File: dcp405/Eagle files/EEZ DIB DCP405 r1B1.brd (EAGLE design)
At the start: 185 x 95 mm, 321 parts, among them IC1 LTC3864EMSE#PBF, IC10 OPA2196ID, IC11 MC33272ADR2G, IC12 LTC2050HVCS8#PBF, IC13 74AUP1G74DC.125, IC14 MCP23S17-E/SS, IC15 REF5025AIDR, IC16 DAC8552IDGKR, IC17 SN74LVC1G3157DCKR, IC18 ADS1120IPWR, IC19 LM339D, IC2 TL783CKCSE3, IC20 MAX9141ESA, IC3 LP2951, IC4 SI8641BB-B-IS1, IC5 SN74LVC1G139DCUR, IC6 LTC3260EMSE#PBF, IC7 SI8641BB-B-IS1, IC8 M24C32-WMN6P, IC9 TMP1075AIDGK, J1 4907, J2 FCR7350R, J3 FCR7350B, K1 G6K-2F-5DC, Q1 SUD19P06-60, Q10 MMBT5551, Q11 MMBT5551, Q12 PSMN0R9-25YLC, Q13 PSMN0R9-25YLC, Q14 PSMN0R9-25YLC, Q15 2N7002, Q16 BSS84P, Q17 BTA26-600, Q18 FMMT493TA, Q19 2N7002, Q2 MMBT5401, Q20 2N7002, Q21 2N7002, Q22 MMBT5551, Q23 MMBT5401, Q24 MMBT5551, Q25 MMBT5551, Q26 2N7002, Q3 IRFP250MPBF, Q4 BC856C, Q5 BCP56-16.115, Q6 STF10P6F6, Q7 BCP56-16.115, Q8 MMBT5401, Q9 MMBT5401, X1 39-30-1020, X2 M20-9701346, X3 1844249, X4 ZL263-20DG

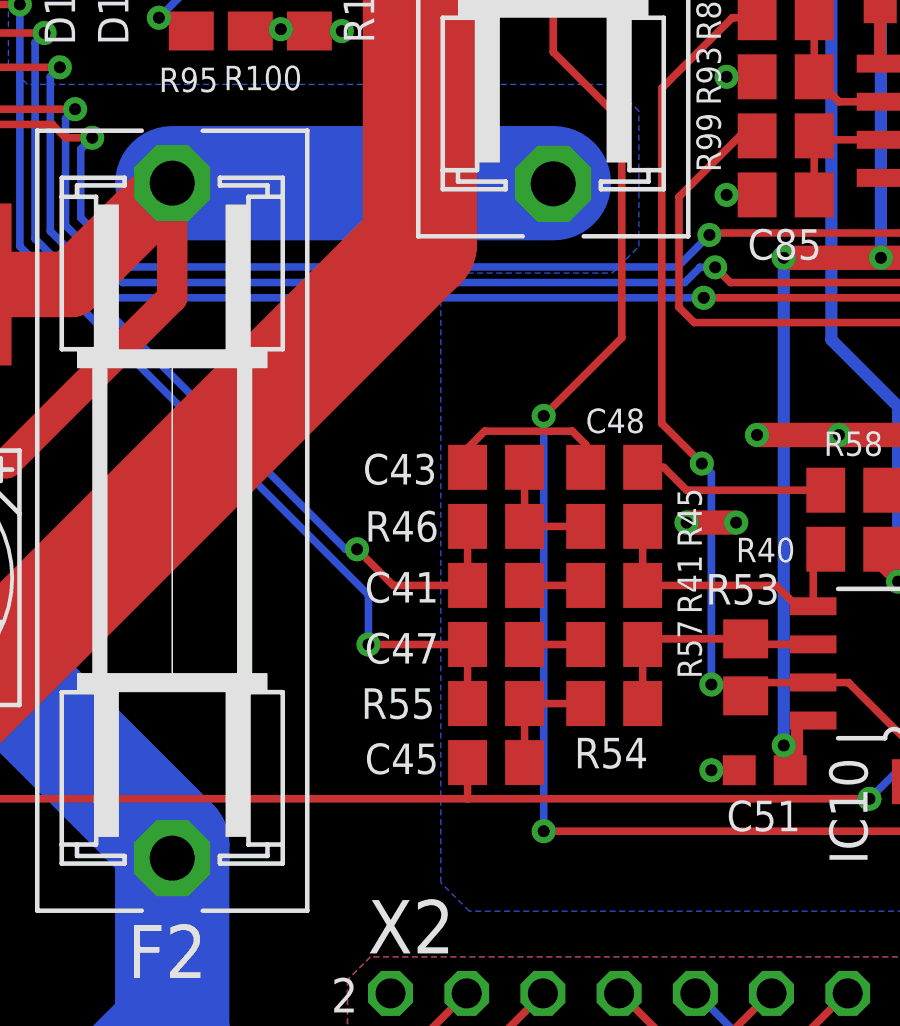
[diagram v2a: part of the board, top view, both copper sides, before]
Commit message: DCP405 JP3, JP4 added
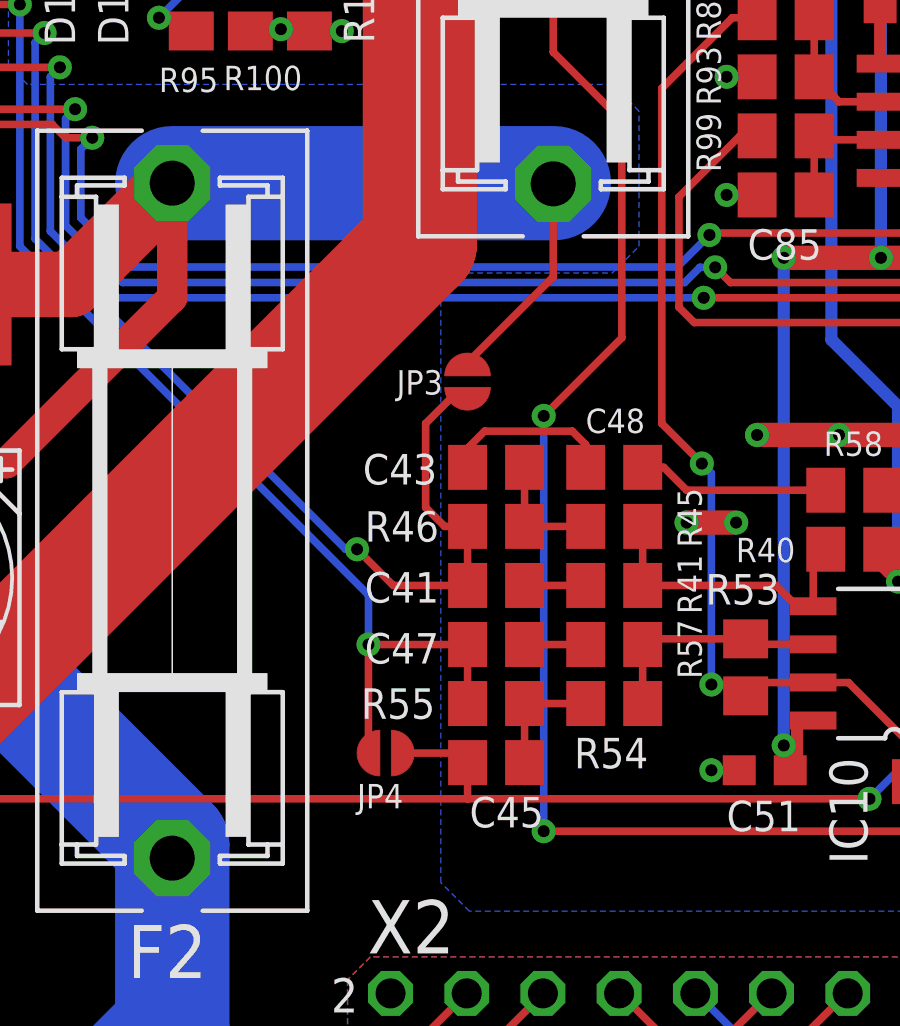
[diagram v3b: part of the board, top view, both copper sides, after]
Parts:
- added JP3, JP4: JP2-CUT, EEZ_Lib1:JP2-CUT
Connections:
- net POST_OUT-: now also JP4.1
- net POST_OUTF+: now also JP3.2
- net SENSE+: now also JP3.1
- net SENSE-: now also JP4.2
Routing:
- net POST_OUTF+: track 97.0 -> 104.2 mm
- net SENSE+: track 72.8 -> 79.1 mm
- net SENSE-: track 71.2 -> 74.8 mm
- net POST_OUT-: track 229.2 -> 231.6 mm
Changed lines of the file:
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@@
 <layer number="24" name="bOrigins" color="15" fill="1" visible="no" active="yes"/>
 <layer number="25" name="tNames" color="7" fill="1" visible="yes" active="yes"/>
-<layer number="26" name="bNames" color="5" fill="1" visible="yes" active="yes"/>
+<layer number="26" name="bNames" color="5" fill="1" visible="no" active="yes"/>
 <layer number="27" name="tValues" color="14" fill="1" visible="no" active="yes"/>
 <layer number="28" name="bValues" color="10" fill="1" visible="no" active="yes"/>
@@
 </element>
 <element name="C45" library="rcl" package="C0805" value="2n2" x="58.039" y="20.193" smashed="yes" rot="R180">
-<attribute name="NAME" x="56.134" y="20.828" size="1.016" layer="25" ratio="10" rot="R180"/>
+<attribute name="NAME" x="59.6265" y="19.05" size="1.016" layer="25" ratio="10" rot="R180"/>
 <attribute name="VALUE" x="59.563" y="20.6375" size="1.016" layer="27" ratio="10" rot="R180"/>
 </element>
@@
 <element name="C66" library="EEZ_Lib1" package="EC1206" value="4u7 tant." x="101.6635" y="24.511" smashed="yes">
 <attribute name="NAME" x="100.33" y="25.781" size="1.016" layer="25" ratio="10"/>
-<attribute name="VALUE" x="100.2665" y="24.003" size="1.016" layer="27" ratio="10"/>
+<attribute name="VALUE" x="99.06" y="24.1935" size="0.8128" layer="27" ratio="10"/>
 </element>
 <element name="C79" library="rcl" package="C0603" value="100n" x="113.6015" y="26.543" smashed="yes" rot="R270">
@@
 <attribute name="TME" value="MCP23S17-E/SS" x="336.804" y="17.653" size="1.778" layer="27" rot="R90" display="off"/>
 <attribute name="NAME" x="144.3101" y="57.9755" size="1.27" layer="25" ratio="10" rot="SR0"/>
-<attribute name="VALUE" x="148.5265" y="53.6829" size="0.8128" layer="27" ratio="10" rot="SR180"/>
+<attribute name="VALUE" x="139.0015" y="52.9336" size="0.8128" layer="27" ratio="10" rot="SR0"/>
 </element>
 <element name="R78" library="rcl" package="R0805" value="270R" x="12.5095" y="31.5265" smashed="yes" rot="R90">
@@
 <element name="C6" library="rcl" package="C1210" value="4u7/100V" x="168.91" y="56.388" smashed="yes" rot="R90">
 <attribute name="NAME" x="168.2115" y="59.055" size="1.016" layer="25" ratio="10"/>
-<attribute name="VALUE" x="169.545" y="54.991" size="1.016" layer="27" ratio="10" rot="R90"/>
+<attribute name="VALUE" x="169.418" y="53.721" size="0.8128" layer="27" ratio="10" rot="R90"/>
 </element>
 <element name="C10" library="rcl" package="C1210" value="10u" x="169.7355" y="67.056" smashed="yes" rot="R270">
@@
 <element name="C5" library="rcl" package="C1210" value="4u7/100V" x="172.1485" y="56.388" smashed="yes" rot="R90">
 <attribute name="NAME" x="171.45" y="59.055" size="1.016" layer="25" ratio="10"/>
-<attribute name="VALUE" x="172.593" y="55.0545" size="1.016" layer="27" ratio="10" rot="R90"/>
+<attribute name="VALUE" x="172.593" y="53.6575" size="0.8128" layer="27" ratio="10" rot="R90"/>
 </element>
 <element name="D2" library="EEZ_Lib1" package="TO252-L" value="STPS15H100" x="158.3055" y="58.6105" smashed="yes" rot="R90">
 <attribute name="NAME" x="154.051" y="59.1185" size="1.27" layer="25" ratio="10" rot="R180"/>
-<attribute name="VALUE" x="165.354" y="59.309" size="1.016" layer="27" ratio="10" rot="R180"/>
+<attribute name="VALUE" x="161.798" y="60.579" size="1.016" layer="27" ratio="10" rot="R180"/>
 </element>
 <element name="R4" library="rcl" package="R0805" value="47K" x="166.243" y="38.4175" smashed="yes" rot="R180">
@@
 <element name="Q1" library="EEZ_Lib1" package="TO229P990X239-3N" value="SUD19P06-60" x="158.3055" y="49.911" smashed="yes" rot="R90">
 <attribute name="NAME" x="154.8765" y="50.546" size="1.27" layer="25" ratio="10" rot="R180"/>
-<attribute name="VALUE" x="161.4805" y="50.4825" size="1.016" layer="27" ratio="10" rot="R180"/>
+<attribute name="VALUE" x="161.6075" y="51.7525" size="1.016" layer="27" ratio="10" rot="R180"/>
 </element>
 <element name="IC1" library="EEZ_Lib1" package="LTC_05-08-1666" value="LTC3864EMSE#PBF" x="170.815" y="42.6085" smashed="yes" rot="R90">
@@
 <element name="FB2" library="EEZ_Lib1" package="BEAD0603" value="60R@100MHz" x="149.1615" y="3.1115" smashed="yes" rot="R180">
 <attribute name="NAME" x="150.627" y="2.648" size="1.016" layer="25" ratio="10"/>
-<attribute name="VALUE" x="147.7505" y="2.7245" size="0.8128" layer="27" ratio="10"/>
+<attribute name="VALUE" x="147.7505" y="2.28" size="0.8128" layer="27" ratio="10"/>
 </element>
 <element name="R21" library="rcl" package="R0805" value="100K" x="157.48" y="9.017" smashed="yes">
@@
 <element name="C4" library="rcl" package="C1206" value="4n7/100V" x="161.29" y="21.2725" smashed="yes" rot="R270">
 <attribute name="NAME" x="158.9405" y="22.7965" size="1.016" layer="25" ratio="10" rot="R270"/>
-<attribute name="VALUE" x="161.8615" y="16.383" size="1.016" layer="27" ratio="10" rot="R90"/>
+<attribute name="VALUE" x="161.671" y="17.907" size="0.8128" layer="27" ratio="10" rot="R90"/>
 </element>
 <element name="C3" library="rcl" package="C1206" value="4n7/100V" x="161.29" y="26.67" smashed="yes" rot="R270">
 <attribute name="NAME" x="161.798" y="29.4005" size="1.27" layer="25" ratio="10" rot="R90"/>
-<attribute name="VALUE" x="160.7185" y="31.8135" size="1.016" layer="27" ratio="10" rot="R270"/>
+<attribute name="VALUE" x="160.782" y="30.226" size="0.8128" layer="27" ratio="10" rot="R270"/>
 </element>
 <element name="C1" library="rcl" package="C1206" value="4n7/100V" x="182.626" y="23.622" smashed="yes" rot="R270">
@@
 <element name="C12" library="rcl" package="C0805" value="n.c." x="162.433" y="85.6615" smashed="yes" rot="R270">
 <attribute name="NAME" x="162.8775" y="87.8205" size="1.016" layer="25" ratio="10" rot="R90"/>
-<attribute name="VALUE" x="162.052" y="87.1855" size="1.27" layer="27" rot="R270"/>
+<attribute name="VALUE" x="161.6075" y="87.5665" size="1.27" layer="27" rot="R270"/>
 </element>
 <element name="C33" library="rcl" package="C1210" value="10u" x="150.4315" y="20.447" smashed="yes">
@@
 <element name="C27" library="EEZ_Lib1" package="EC1206" value="10u tant." x="155.6385" y="4.3815" smashed="yes">
 <attribute name="NAME" x="158.242" y="4.0005" size="1.016" layer="25" ratio="10"/>
-<attribute name="VALUE" x="156.7815" y="4.7625" size="1.016" layer="27" ratio="10" rot="R180"/>
+<attribute name="VALUE" x="153.4795" y="3.937" size="1.016" layer="27" ratio="10"/>
 </element>
 <element name="C34" library="EEZ_Lib1" package="EC1206" value="10u tant." x="155.6385" y="21.9075" smashed="yes" rot="R180">
 <attribute name="NAME" x="153.162" y="23.114" size="1.016" layer="25" ratio="10"/>
-<attribute name="VALUE" x="157.2895" y="22.4155" size="1.27" layer="27" ratio="10" rot="R180"/>
+<attribute name="VALUE" x="159.3215" y="22.4155" size="0.8128" layer="27" ratio="10" rot="R180"/>
 </element>
 <element name="C21" library="rcl" package="C0603" value="100n" x="157.4165" y="37.846" smashed="yes" rot="R270">
@@
 <attribute name="NAME" x="72.771" y="29.7815" size="0.8128" layer="25" ratio="10"/>
 </element>
+<element name="JP3" library="EEZ_Lib1" package="JP2-CUT" value="JP2-CUT" x="57.0865" y="32.893" smashed="yes" rot="R90">
+<attribute name="NAME" x="56.261" y="33.274" size="0.8128" layer="25" ratio="10" rot="R180"/>
+</element>
+<element name="JP4" library="EEZ_Lib1" package="JP2-CUT" value="JP2-CUT" x="54.356" y="20.5105" smashed="yes" rot="R180">
+<attribute name="NAME" x="53.4035" y="18.669" size="0.8128" layer="25" ratio="10"/>
+</element>
 </elements>
 <signals>
@@
 <wire x1="20.193" y1="48.3235" x2="36.957" y2="48.3235" width="0.254" layer="1"/>
 <wire x1="39.8145" y1="45.466" x2="36.957" y2="48.3235" width="0.254" layer="1"/>
+<contactref element="JP4" pad="2"/>
+<wire x1="53.721" y1="20.5105" x2="53.7845" y2="20.5105" width="0.254" layer="1"/>
+<wire x1="53.7845" y1="20.5105" x2="53.7845" y2="24.13" width="0.254" layer="1"/>
 </signal>
 <signal name="SENSE+">
@@
 <wire x1="19.939" y1="47.8155" x2="36.6395" y2="47.8155" width="0.254" layer="1"/>
 <wire x1="36.6395" y1="47.8155" x2="39.9415" y2="44.5135" width="0.254" layer="1"/>
+<contactref element="JP3" pad="1"/>
+<wire x1="57.089" y1="28.067" x2="56.3245" y2="28.067" width="0.254" layer="1"/>
+<wire x1="56.3245" y1="28.067" x2="55.6895" y2="28.702" width="0.254" layer="1"/>
+<wire x1="55.6895" y1="28.702" x2="55.6895" y2="31.496" width="0.254" layer="1"/>
+<wire x1="55.6895" y1="31.496" x2="56.5785" y2="32.385" width="0.254" layer="1"/>
+<wire x1="56.5785" y1="32.385" x2="56.9595" y2="32.385" width="0.254" layer="1"/>
+<wire x1="56.9595" y1="32.385" x2="57.0865" y2="32.258" width="0.254" layer="1"/>
 </signal>
 <signal name="N$83">
@@
 <wire x1="55.6895" y1="69.0245" x2="55.499" y2="69.215" width="0.254" layer="1"/>
 <wire x1="57.0865" y1="18.9865" x2="40.3225" y2="18.9865" width="0.254" layer="1"/>
+<contactref element="JP4" pad="1"/>
+<wire x1="54.991" y1="20.5105" x2="57.089" y2="20.5105" width="0.254" layer="1"/>
+<wire x1="57.089" y1="20.5105" x2="57.089" y2="20.193" width="0.254" layer="1"/>
 </signal>
 <signal name="N$86">
@@
 <wire x1="30.988" y1="55.245" x2="30.988" y2="52.6415" width="0.254" layer="1"/>
 <wire x1="30.988" y1="52.6415" x2="33.4645" y2="50.165" width="0.254" layer="1"/>
+<contactref element="JP3" pad="2"/>
 <wire x1="59.965" y1="39.5075" x2="59.944" y2="39.4865" width="0" layer="19" extent="16-16"/>
+<wire x1="59.944" y1="39.4865" x2="59.944" y2="36.3855" width="0.254" layer="1"/>
+<wire x1="59.944" y1="36.3855" x2="57.0865" y2="33.528" width="0.254" layer="1"/>
 </signal>
 <signal name="DIB_NFAULT">
